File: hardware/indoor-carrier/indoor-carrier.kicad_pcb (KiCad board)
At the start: 2 copper layers, 100 x 80 mm, 29 parts, among them J1 24 VAC, J2 Mode in 24 VAC, J3 DS18B20 supply air, J4 DS18B20 return air, J5 I2C expansion, U1 ESP32 DevKit, U2 LM2596HV, U3 H11AA1, U4 H11AA1, U5 H11AA1, U6 H11AA1

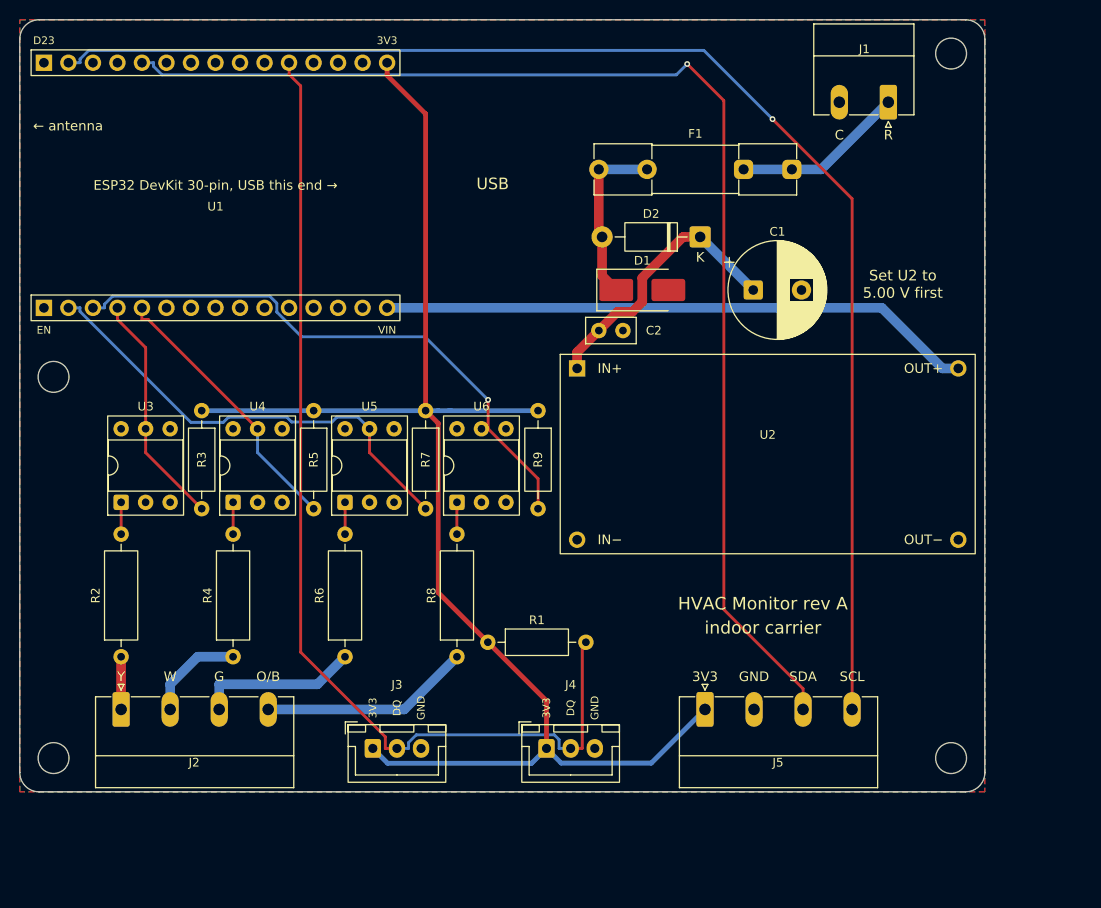
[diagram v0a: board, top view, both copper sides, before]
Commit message: Rev B layout: place, route and fab both carrier boards (DRC clean)
Boards: outdoor 110 x 110 mm, indoor 110 x 90 mm (both fit the Hammond 1554R2GY).
The top band is the same on both: the ESP32 (antenna keepout kept), the Wio-SX1262 at
the top edge with its u.FL toward the top wall, the AMS1117 and its caps, SW1 SETUP, and
the rev A power corner moved 10 mm right.
- Outdoor: CT jacks J11-J13 on the left edge. The footprint's own Edge.Cuts nose notch
  is part of the outline, using an edge-silk-trimmed copy in hvac_carrier. The CT
  passives (now 0805) and CT_BIAS sit beside the jacks. The ADS block is next to them,
  with the dividers and thermistor refs in 3.5 mm columns. The mode inputs are on the
  right, and J3-J10 are along the bottom.
- Indoor: TCA9548A, mux jacks J6-J10 along the bottom edge with their pull-ups,
  DS18B20 jacks on the left edge, and J5 on the right edge.
- preroute.py: the rev A hand routes no longer fit, so it is empty. route.py adds
  locked ground fan-out vias for SMD GND pads and a stitching via grid. It fixes
  starved GND thermals (45 degree spokes, then solid) and checks the result with
  kicad-cli. It also fixes a use-after-delete in the duplicate-track pass.
- route-all.sh retries Freerouting until DRC is clean. make_fab.py writes the
  gerbers zip, BOM, renders, schematic PDF, erc.rpt and drc.rpt.
DRC: 0 violations, 0 unconnected, 0 footprint errors (all severities, schematic
parity) on both boards. ERC: 0 errors, 0 warnings.

Co-Authored-By: Claude Opus 5.5 (1M context) <noreply@anthropic.com>
Claude-Session: https://claude.ai/code/session_01V4kWJ9CiBrt94u4WqUxFsk
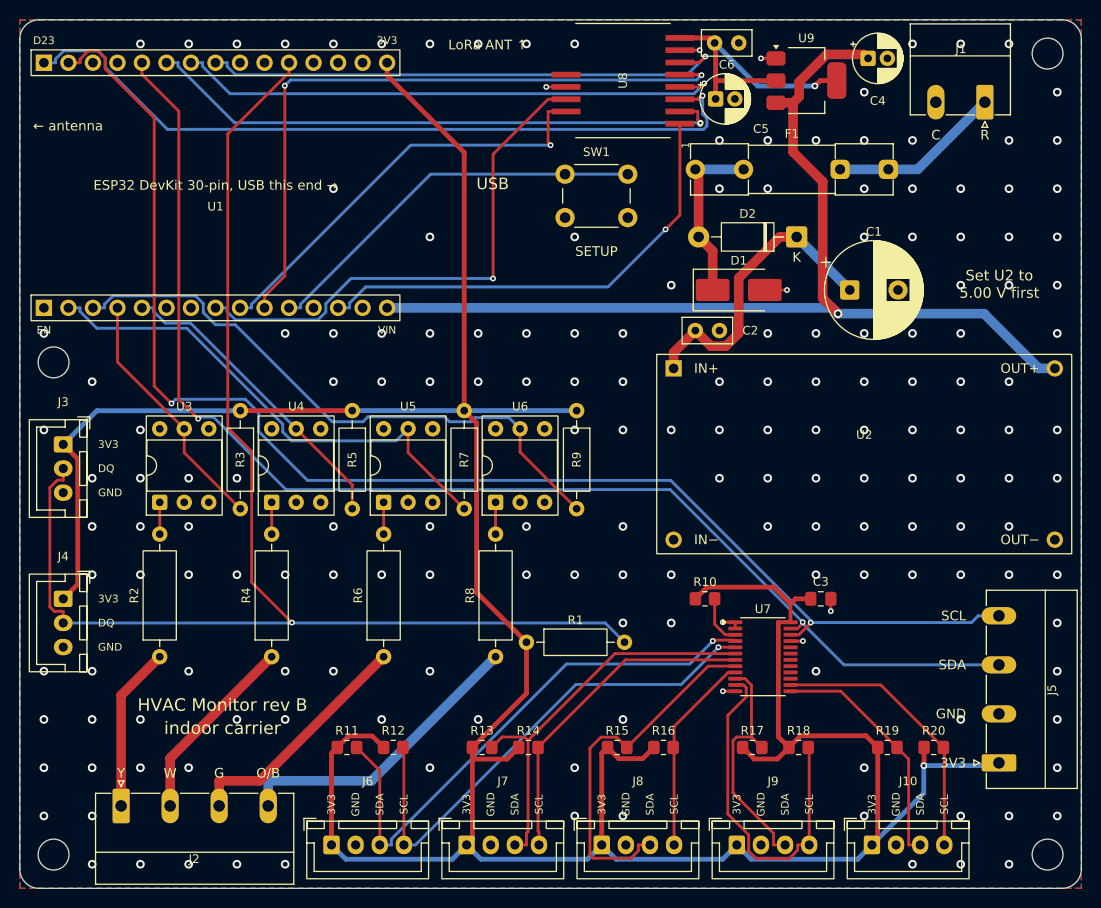
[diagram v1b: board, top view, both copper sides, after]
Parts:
- added C3: 0.1µF, Capacitor_SMD:C_0805_2012Metric_Pad1.18x1.45mm_HandSolder, F.Cu at (133.0, 110.0)
- added C4: 10µF 16V, Capacitor_THT:CP_Radial_D5.0mm_P2.00mm, F.Cu at (137.9, 54.0)
- added C5: 22µF 10V, Capacitor_THT:CP_Radial_D5.0mm_P2.00mm, F.Cu at (122.1, 58.2)
- added C6: 0.1µF, Capacitor_THT:C_Disc_D5.0mm_W2.5mm_P2.50mm, F.Cu at (122.0, 52.4)
- added J10: SDP810 filter, Connector_JST:JST_XH_B4B-XH-A_1x04_P2.50mm_Vertical, F.Cu at (138.3, 135.5)
- added J6: SHT45 return, Connector_JST:JST_XH_B4B-XH-A_1x04_P2.50mm_Vertical, F.Cu at (82.3, 135.5)
- added J7: SHT45 supply, Connector_JST:JST_XH_B4B-XH-A_1x04_P2.50mm_Vertical, F.Cu at (96.3, 135.5)
- added J8: SDP810 return, Connector_JST:JST_XH_B4B-XH-A_1x04_P2.50mm_Vertical, F.Cu at (110.3, 135.5)
- added J9: SDP810 supply, Connector_JST:JST_XH_B4B-XH-A_1x04_P2.50mm_Vertical, F.Cu at (124.3, 135.5)
- added R10: 10k, Resistor_SMD:R_0805_2012Metric_Pad1.20x1.40mm_HandSolder, F.Cu at (121.0, 110.0)
- added R11: 10k, Resistor_SMD:R_0805_2012Metric_Pad1.20x1.40mm_HandSolder, F.Cu at (83.9, 125.4)
- added R12: 10k, Resistor_SMD:R_0805_2012Metric_Pad1.20x1.40mm_HandSolder, F.Cu at (88.7, 125.4)
- added R13: 10k, Resistor_SMD:R_0805_2012Metric_Pad1.20x1.40mm_HandSolder, F.Cu at (97.9, 125.4)
- added R14: 10k, Resistor_SMD:R_0805_2012Metric_Pad1.20x1.40mm_HandSolder, F.Cu at (102.7, 125.4)
- added R15: 10k, Resistor_SMD:R_0805_2012Metric_Pad1.20x1.40mm_HandSolder, F.Cu at (111.9, 125.4)
- added R16: 10k, Resistor_SMD:R_0805_2012Metric_Pad1.20x1.40mm_HandSolder, F.Cu at (116.7, 125.4)
- added R17: 10k, Resistor_SMD:R_0805_2012Metric_Pad1.20x1.40mm_HandSolder, F.Cu at (125.9, 125.4)
- added R18: 10k, Resistor_SMD:R_0805_2012Metric_Pad1.20x1.40mm_HandSolder, F.Cu at (130.7, 125.4)
- added R19: 10k, Resistor_SMD:R_0805_2012Metric_Pad1.20x1.40mm_HandSolder, F.Cu at (139.9, 125.4)
- added R20: 10k, Resistor_SMD:R_0805_2012Metric_Pad1.20x1.40mm_HandSolder, F.Cu at (144.7, 125.4)
- added SW1: SETUP, Button_Switch_THT:SW_PUSH_6mm, F.Cu at (106.5, 66.0)
- added U7: TCA9548A, Package_SO:TSSOP-24_4.4x7.8mm_P0.65mm, F.Cu at (127.0, 116.0)
- added U8: Wio-SX1262, hvac_carrier:Wio_SX1262, F.Cu at (112.5, 56.3)
- added U9: AMS1117-3.3, Package_TO_SOT_SMD:SOT-223-3_TabPin2, F.Cu at (131.5, 56.3)
- moved J4 52.4 mm to (54.5, 110.0), turned to -90 degrees
- moved J3 45.0 mm to (54.5, 94.0), turned to -90 degrees
- moved J5 31.0 mm to (151.5, 127.0), turned to 90 degrees
- moved H3 14.1 mm to (156.5, 136.5)
- moved J2 10.0 mm to (60.5, 131.5)
- moved C1 10.0 mm to (136.0, 78.0)
- moved C2 10.0 mm to (120.0, 82.2)
- moved D1 10.0 mm to (124.5, 78.0)
- moved D2 10.0 mm to (130.5, 72.5)
- moved F1 10.0 mm to (140.0, 65.5)
- moved H2 10.0 mm to (53.5, 136.5)
- moved H4 10.0 mm to (156.5, 53.5)
- moved J1 10.0 mm to (150.0, 58.5)
- moved U2 10.0 mm to (137.5, 95.0)
- moved R1 4.00 mm to (102.5, 114.5)
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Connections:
- U1 pad 10: unconnected-(U1-D27-Pad10) -> /LORA_NRST
- U1 pad 11: unconnected-(U1-D14-Pad11) -> /SETUP
- U1 pad 13: unconnected-(U1-D13-Pad13) -> /LORA_RFSW
- U1 pad 16: unconnected-(U1-D23-Pad16) -> /LORA_MOSI
- U1 pad 21: unconnected-(U1-D19-Pad21) -> /LORA_MISO
- U1 pad 22: unconnected-(U1-D18-Pad22) -> /LORA_SCK
- U1 pad 23: unconnected-(U1-D5-Pad23) -> /LORA_NSS
- U1 pad 8: unconnected-(U1-D25-Pad8) -> /LORA_BUSY
- U1 pad 9: unconnected-(U1-D26-Pad9) -> /LORA_DIO1
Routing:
- net +3V3: track 151.9 -> 336.5 mm, vias 0 -> 1
- net /LORA_MOSI: track 0.00 -> 79.3 mm, vias 0 -> 1
- net /LORA_NRST: track 0.00 -> 69.8 mm, vias 0 -> 2
- net /LORA_MISO: track 0.00 -> 61.3 mm, vias 0 -> 1
- net /LORA_SCK: track 0.00 -> 57.9 mm, vias 0 -> 1
- net /SD0: track 0.00 -> 57.1 mm, vias 0 -> 1
- net /LORA_NSS: track 0.00 -> 55.2 mm, vias 0 -> 1
- net /LORA_BUSY: track 0.00 -> 54.6 mm, vias 0 -> 1
- net /SC0: track 0.00 -> 53.0 mm, vias 0 -> 1
- net /LORA_RFSW: track 0.00 -> 49.2 mm, vias 0 -> 1
- net +5V: track 61.8 -> 108.3 mm, vias 0 -> 1
- net /LORA_DIO1: track 0.00 -> 44.8 mm, vias 0 -> 1
- net /SD1: track 0.00 -> 41.7 mm
- net /SETUP: track 0.00 -> 41.1 mm
- net /SD2: track 0.00 -> 37.8 mm
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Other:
- board size 100 x 80 mm -> 110 x 90 mm
- board text added: "HVAC Monitor rev B"
- board text added: "LoRa ANT ↑"
- board text added: "SETUP"
- board text removed: "HVAC Monitor rev A"

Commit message: Shrink rev B boards with the same parts: outdoor 100 x 100, indoor 100 x 88
The power corner is back at its rev A position. The radio's regulator, input cap and the
SETUP button moved right of C1, so the top band fits in 100 mm.
- Outdoor: the empty band is gone. The dividers sit under U2 in 3.5 mm columns, and the
  thermistor reference resistors sit under U4. Within JLCPCB's cheapest 100 x 100 size again.
- Indoor: J5 sits under U2 on the right edge and H3 is inside the board. The mux chip
  and pull-ups are under U2, and the U6 and 1-Wire pull-ups sit below the optos.
Both boards: DRC 0 violations, 0 unconnected, 0 footprint errors; ERC 0 / 0.
Box, plate and docs updated for the new sizes and holes; SETUP plunger moved with SW1.

Co-Authored-By: Claude Opus 5.5 (1M context) <noreply@anthropic.com>
Claude-Session: https://claude.ai/code/session_01V4kWJ9CiBrt94u4WqUxFsk
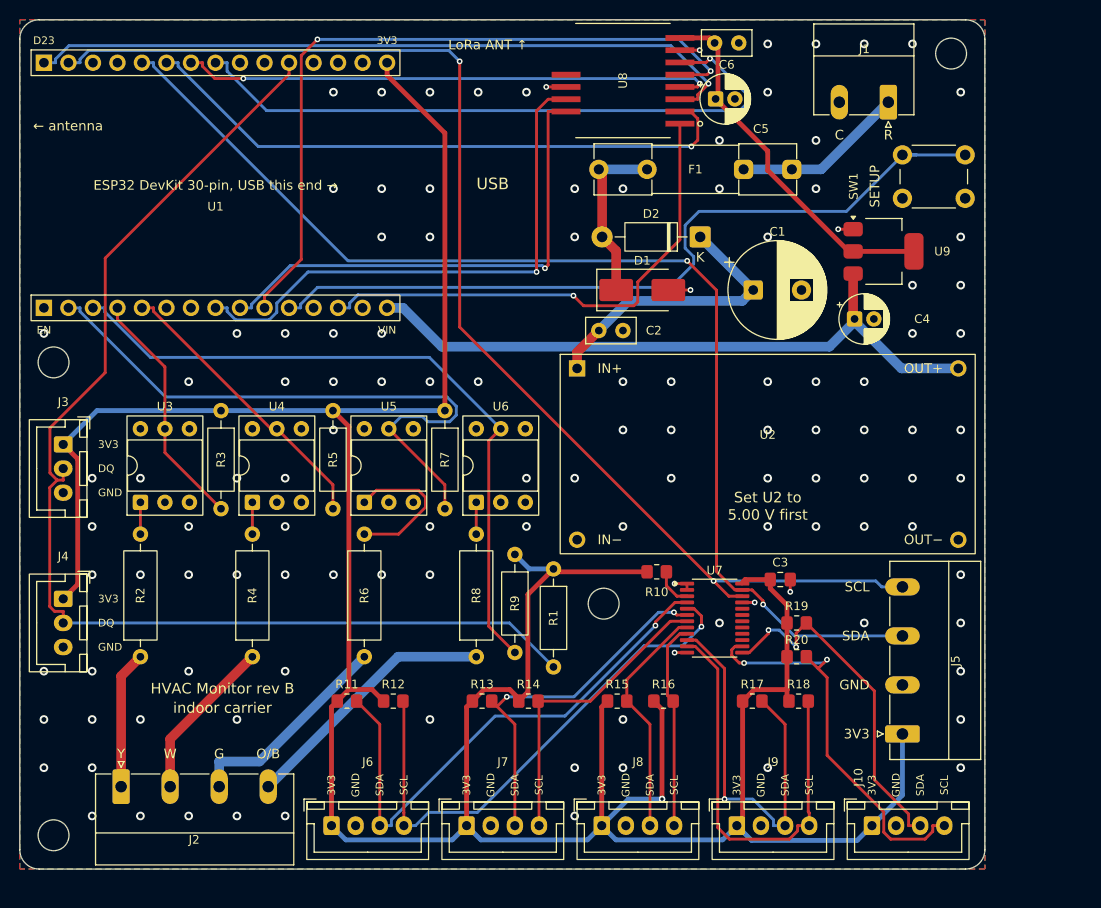
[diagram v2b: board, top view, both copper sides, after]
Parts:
- moved H3 52.8 mm to (110.5, 110.5)
- moved SW1 35.0 mm to (141.5, 64.0)
- moved C4 27.0 mm to (136.5, 81.0)
- moved U9 19.4 mm to (139.5, 74.0)
- moved R20 17.0 mm to (130.5, 116.0)
- moved R9 16.2 mm to (101.3, 105.4)
- moved R19 16.0 mm to (130.5, 112.5)
- moved J5 10.4 mm to (141.5, 124.0)
- moved C1 10.0 mm to (126.0, 78.0)
- moved C2 10.0 mm to (110.0, 82.2)
- moved D1 10.0 mm to (114.5, 78.0)
- moved D2 10.0 mm to (120.5, 72.5)
- moved F1 10.0 mm to (130.0, 65.5)
- moved H4 10.0 mm to (146.5, 53.5)
- moved J1 10.0 mm to (140.0, 58.5)
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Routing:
- net /SETUP: track 41.1 -> 81.9 mm
- net +5V: track 108.3 -> 69.0 mm, vias 1 -> 0
- net /ONEWIRE: track 140.6 -> 124.6 mm, vias 1 -> 0
- net /SD3: track 24.7 -> 40.3 mm, vias 0 -> 1
- net /SC4: track 28.7 -> 42.5 mm, vias 0 -> 2
- net /SDA: track 134.7 -> 120.9 mm
- net /SCL: track 143.2 -> 129.9 mm
- net /SD2: track 37.8 -> 24.6 mm
- net /G_OPTO: track 3.30 -> 15.7 mm
- net /LORA_NSS: track 55.2 -> 67.5 mm
- net /SD4: track 25.2 -> 37.0 mm, vias 0 -> 2
- net /MODE_G: track 52.8 -> 64.2 mm
- net /MODE_OB: track 62.7 -> 72.5 mm
- net /+3V3_RF: track 30.6 -> 38.1 mm, vias 1 -> 0
- net /LORA_DIO1: track 44.8 -> 52.0 mm
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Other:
- board size 110 x 90 mm -> 100 x 88 mm
